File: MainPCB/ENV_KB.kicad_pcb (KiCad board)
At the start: 2 copper layers, 354.6 x 156.2 mm, 201 parts

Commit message: swapped footprint of various parts, updated the logo and tweaked some traces
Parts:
- removed G***: LOGO, EM_Extras:Pattern-Silkscreen
- removed G***: LOGO, EM_Logo:KBLogo
- added D89: 1n4002, Diode_THT:D_DO-35_SOD27_P7.62mm_Horizontal, F.Cu at (227.9, 61.3)
- added kibuzzard-628ADF99 (x2): G***, kibuzzard-628ADF99, F.Cu at (335.3, 172.7)
- added kibuzzard-628AE061 (x3): G***, kibuzzard-628AE061, F.Cu at (357.1, 168.5)
- added kibuzzard-628AE768: G***, kibuzzard-628AE768, F.Cu at (202.7, 66.2)
- added kibuzzard-628AE7EF: G***, kibuzzard-628AE7EF, F.Cu at (310.1, 69.6)
- added kibuzzard-628AE7FB: G***, kibuzzard-628AE7FB, F.Cu at (310.5, 67.0)
- added kibuzzard-628AE805: G***, kibuzzard-628AE805, F.Cu at (310.2, 64.5)
- added kibuzzard-628AE80F: G***, kibuzzard-628AE80F, F.Cu at (310.3, 61.9)
- added kibuzzard-628AE82F: G***, kibuzzard-628AE82F, F.Cu at (320.8, 64.2)
- added kibuzzard-628AE860: G***, kibuzzard-628AE860, F.Cu at (44.3, 69.2)
- added kibuzzard-628AE868: G***, kibuzzard-628AE868, F.Cu at (44.2, 73.2)
- added kibuzzard-628AE874: G***, kibuzzard-628AE874, F.Cu at (44.9, 77.2)
- added kibuzzard-628AE882: G***, kibuzzard-628AE882, F.Cu at (45.0, 81.2)
- added kibuzzard-628AE8A6: G***, kibuzzard-628AE8A6, F.Cu at (44.9, 85.2)
- added kibuzzard-628AE933: G***, kibuzzard-628AE933, F.Cu at (44.8, 89.2)
- added kibuzzard-628AE966: G***, kibuzzard-628AE966, F.Cu at (62.7, 69.2)
- added kibuzzard-628AEA3B: G***, kibuzzard-628AEA3B, F.Cu at (175.4, 64.9)
- added kibuzzard-628AEA3B: G***, kibuzzard-628AEA3B, F.Cu at (180.7, 64.9)
- added kibuzzard-628AEA57: G***, kibuzzard-628AEA57, F.Cu at (186.0, 64.8)
- added kibuzzard-628AEA91: G***, kibuzzard-628AEA91, F.Cu at (202.7, 67.5)
- PowerLED0: value LED 0402 -> LED 3mm; footprint LED_SMD:LED_0402_1005Metric -> LED_THT:LED_D3.0mm
- PowerLedResistor0: value 47K Resistor 0402 -> 47K Resistor; footprint Resistor_SMD:R_0402_1005Metric -> Resistor_THT:R_Axial_DIN0207_L6.3mm_D2.5mm_P7.62mm_Horizontal
- RESISTOR0, RESISTOR1: value 5.1kohm 0402 -> 5.1k; footprint Resistor_SMD:R_0402_1005Metric -> Resistor_THT:R_Axial_DIN0207_L6.3mm_D2.5mm_P7.62mm_Horizontal
- moved RESISTOR1 31.8 mm to (172.7, 62.2), turned to -45 degrees
- moved RESISTOR0 19.2 mm to (183.4, 67.6), turned to 135 degrees
- moved PowerLedResistor0 12.6 mm to (188.6, 67.6), turned to 135 degrees
- moved PowerLED0 7.67 mm to (202.7, 61.5)
- moved kibuzzard-6250C4E7 0.93 mm to (371.0, 62.7)
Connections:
- RPI0 pad 39: unconnected-(RPI0-Pad39) -> VSYS
- RPI0 pad 40: USBVBUS -> unconnected-(RPI0-Pad40)
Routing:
- net GND: track 42.9 -> 76.0 mm, vias 6 -> 5
- net Net-(RESISTOR1-Pad2): track 11.9 -> 38.8 mm
- net Net-(PowerLED0-Pad2): track 1.33 -> 20.7 mm
- net Net-(RESISTOR0-Pad1): track 10.8 -> 29.8 mm
- net USBVBUS: track 29.5 -> 40.8 mm, vias 3 -> 2
- net col15: track 185.1 -> 179.5 mm
- net col4: track 248.1 -> 245.7 mm
- net col2: track 276.3 -> 274.3 mm
- net col0: track 345.0 -> 343.0 mm
- net USB2_N: track 45.2 -> 43.3 mm
- net Net-(D62-Pad2): track 134.2 -> 132.6 mm
- net col6: track 232.4 -> 231.0 mm
- net USB2_P: track 44.9 -> 43.5 mm
- net col10: track 182.2 -> 181.0 mm
- net col3: track 282.7 -> 281.8 mm
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- added copper zone on F.Cu, net (none)
- added copper zone on F.Cu, net VSYS
- removed copper zone on F.Cu, net USBVBUS
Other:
- board text removed: "PWR"
- board text removed: "RESET"

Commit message: various trace tweaks to make the board look more consistent
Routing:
- net USB2_N: track 43.3 -> 48.8 mm
- net Net-(D76-Pad2): track 157.1 -> 161.6 mm
- net Net-(D84-Pad2): track 171.2 -> 175.6 mm
- net Net-(D62-Pad2): track 132.6 -> 136.7 mm
- net Net-(D61-Pad2): track 138.6 -> 142.1 mm
- net Net-(D63-Pad2): track 118.0 -> 121.3 mm
- net Net-(D45-Pad2): track 95.3 -> 98.6 mm
- net Net-(D51-Pad2): track 102.9 -> 106.1 mm
- net Net-(D30-Pad2): track 68.9 -> 72.1 mm
- net Net-(D44-Pad2): track 102.5 -> 105.3 mm
- net Net-(D28-Pad2): track 83.1 -> 85.9 mm
- net Net-(D9-Pad2): track 43.3 -> 45.7 mm
- net Net-(D0-Pad2): track 10.7 -> 12.7 mm
- net Net-(D46-Pad2): track 108.7 -> 110.7 mm
- net Net-(D78-Pad2): track 145.1 -> 146.8 mm
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
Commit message: small tweaks
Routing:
- net Net-(D76-Pad2): track 161.6 -> 167.5 mm
- net USB2_N: track 48.8 -> 52.3 mm
- net Net-(D81-Pad2): track 148.8 -> 147.7 mm
- net Net-(D65-Pad2): track 115.3 -> 116.3 mm
- net Net-(D62-Pad2): track 136.7 -> 135.8 mm
- net col2: track 274.3 -> 275.1 mm
- net col14: track 181.3 -> 181.9 mm
- net Net-(D12-Pad2): track 25.5 -> 26.0 mm

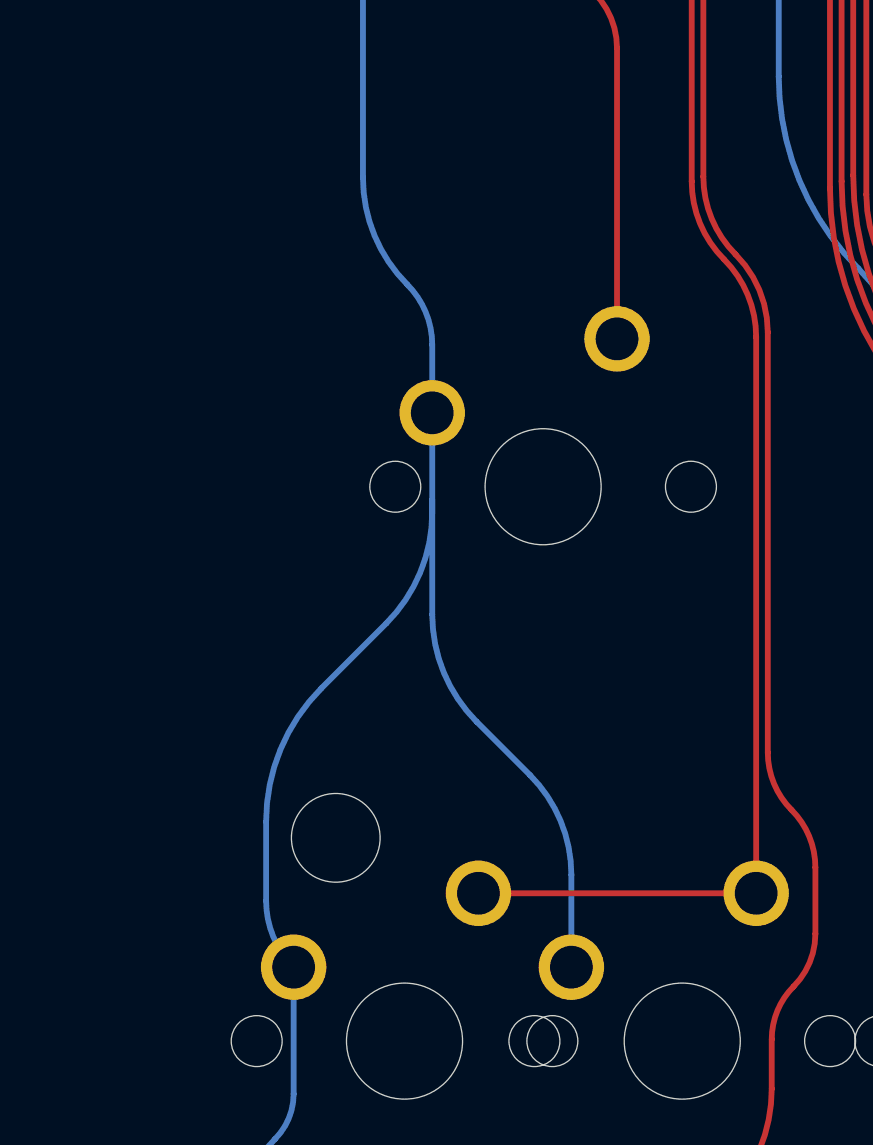
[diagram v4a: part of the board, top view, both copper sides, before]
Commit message: Added Stepped left shift for orig version
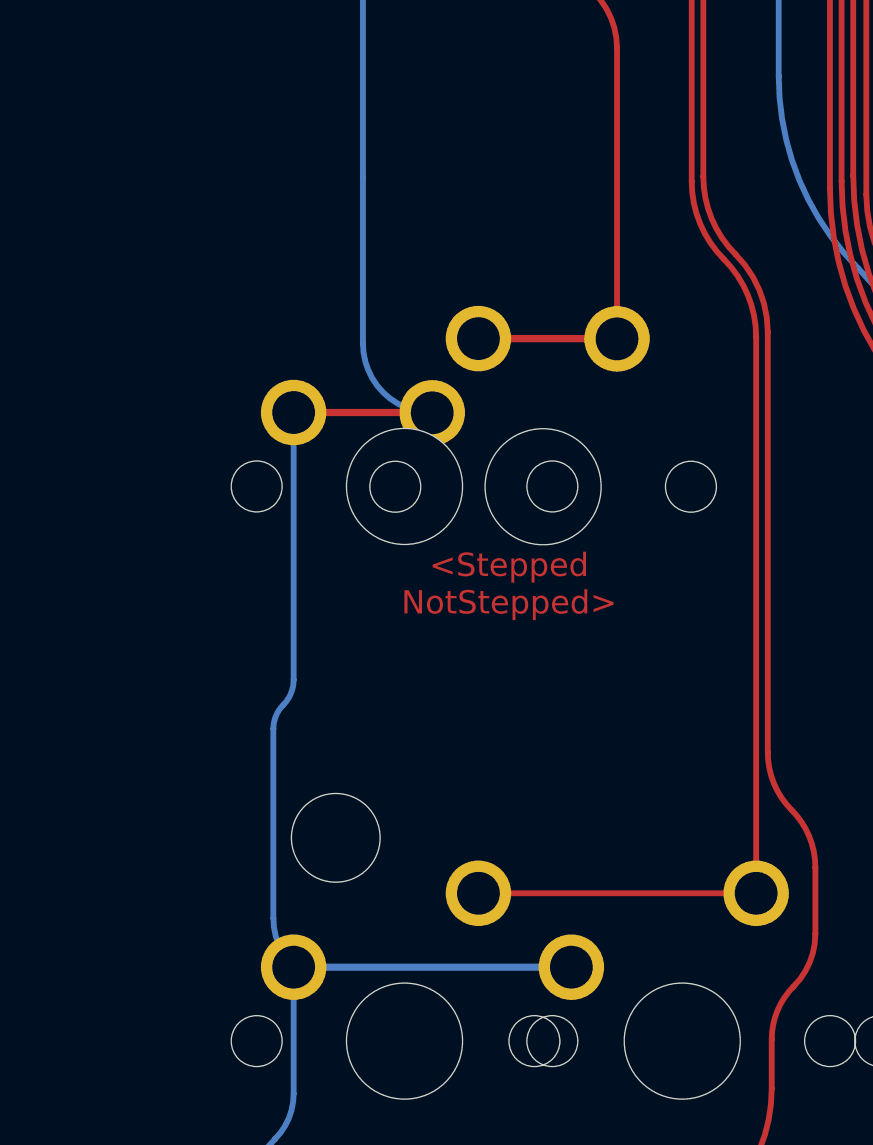
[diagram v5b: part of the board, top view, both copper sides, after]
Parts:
- added K_50A1: KEYSW, MX_Only:MXOnly-1.25U-NoLED, F.Cu at (49.1, 168.4)
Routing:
- net Net-(D50-Pad2): track 95.3 -> 100.0 mm
- net col0: track 343.1 -> 338.9 mm
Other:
- board text added: "<Stepped NotStepped>"
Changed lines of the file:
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@@
       ) (layer "F.SilkS") (width 0) (fill solid))
   )
+  (footprint "MX_Only:MXOnly-1.25U-NoLED" (layer "F.Cu")
+    (at 49.10625 168.45)
+    (property "Sheetfile" "ENV_KB.kicad_sch")
+    (property "Sheetname" "")
+    (attr through_hole)
+    (fp_text reference "K_50A1" (at 0 3.175) (layer "Dwgs.User")
+      (effects (font (size 1 1) (thickness 0.15)))
+    )
+    (fp_text value "KEYSW" (at 0 -7.9375) (layer "Dwgs.User")
+      (effects (font (size 1 1) (thickness 0.15)))
+    )
+    (fp_line (start -7 -7) (end -7 -5) (layer "Dwgs.User") (width 0.15))
+    (fp_line (start -11.90625 -9.525) (end 11.90625 -9.525) (layer "Dwgs.User") (width 0.15))
+    (fp_line (start -5 -7) (end -7 -7) (layer "Dwgs.User") (width 0.15))
+    (fp_line (start -7 5) (end -7 7) (layer "Dwgs.User") (width 0.15))
+    (fp_line (start 5 -7) (end 7 -7) (layer "Dwgs.User") (width 0.15))
+    (fp_line (start -7 7) (end -5 7) (layer "Dwgs.User") (width 0.15))
+    (fp_line (start 5 7) (end 7 7) (layer "Dwgs.User") (width 0.15))
+    (fp_line (start -11.90625 9.525) (end -11.90625 -9.525) (layer "Dwgs.User") (width 0.15))
+    (fp_line (start 7 -7) (end 7 -5) (layer "Dwgs.User") (width 0.15))
+    (fp_line (start 11.90625 -9.525) (end 11.90625 9.525) (layer "Dwgs.User") (width 0.15))
+    (fp_line (start -11.90625 9.525) (end 11.90625 9.525) (layer "Dwgs.User") (width 0.15))
+    (fp_line (start 7 7) (end 7 5) (layer "Dwgs.User") (width 0.15))
+    (pad "" np_thru_hole circle locked (at 5.08 0 48.0996) (size 1.75 1.75) (drill 1.75) (layers *.Cu *.Mask))
+    (pad "" np_thru_hole circle locked (at 0 0) (size 3.9878 3.9878) (drill 3.9878) (layers *.Cu *.Mask))
+    (pad "" np_thru_hole circle locked (at -5.08 0 48.0996) (size 1.75 1.75) (drill 1.75) (layers *.Cu *.Mask))
+    (pad "1" thru_hole circle locked (at -3.81 -2.54) (size 2.25 2.25) (drill 1.47) (layers *.Cu *.Mask)
+      (net 1 "col0") (pinfunction "COL") (pintype "passive"))
+    (pad "2" thru_hole circle locked (at 2.54 -5.08) (size 2.25 2.25) (drill 1.47) (layers *.Cu *.Mask)
+      (net 67 "Net-(D50-Pad2)") (pinfunction "ROW") (pintype "passive"))
+  )
   (footprint "MountingHole:MountingHole_2.2mm_M2_Pad" (layer "F.Cu")
     (at 192.325 63.385)
@@
   (gr_line (start 246.625 78.635) (end 243.125 78.635) (layer "Edge.Cuts") (width 0.1))
   (gr_line (start 216.92804 60.188128) (end 216.925 59.635) (layer "Edge.Cuts") (width 0.1))
+  (gr_text "<Stepped\nNotStepped>" (at 52.7 171.8) (layer "F.Cu")
+    (effects (font (size 0.8 0.8) (thickness 0.15)))
+  )
   (gr_text "https://github.com/Envious-Data/Env-KB" (at 256.225 74.735) (layer "B.Cu")
     (effects (font (size 1 1) (thickness 0.2)) (justify right mirror))
@@
     (style (thickness 0.1) (arrow_length 1.27) (text_position_mode 0) (extension_height 0.58642) (extension_offset 0) keep_text_aligned)
   )
+  (segment (start 45.29625 165.91) (end 50.04875 165.91) (width 0.25) (layer "F.Cu") (net 1))
+  (segment (start 50.04875 165.91) (end 50.05875 165.92) (width 0.25) (layer "F.Cu") (net 1))
+  (segment (start 45.29625 175.09625) (end 45.29625 165.91) (width 0.2) (layer "B.Cu") (net 1))
   (segment (start 244.298792 89.841207) (end 250.54 83.6) (width 0.2) (layer "B.Cu") (net 1))
-  (segment (start 54.84 184.97) (end 54.84 181.799183) (width 0.2) (layer "B.Cu") (net 1))
-  (segment (start 53.42 178.371) (end 51.586454 176.537454) (width 0.2) (layer "B.Cu") (net 1))
+  (segment (start 47.6775 163.53875) (end 47.6775 157.83436) (width 0.2) (layer "B.Cu") (net 1))
   (segment (start 47.915 91.435) (end 240.451036 91.435) (width 0.2) (layer "B.Cu") (net 1))
+  (segment (start 54.84 184.97) (end 45.29625 184.97) (width 0.25) (layer "B.Cu") (net 1))
   (segment (start 42.915 127.82) (end 42.915 99.245) (width 0.2) (layer "B.Cu") (net 1))
-  (segment (start 44.35 182.685551) (end 44.35 179.969871) (width 0.2) (layer "B.Cu") (net 1))
-  (segment (start 50.05875 172.84925) (end 50.05875 168.90125) (width 0.2) (layer "B.Cu") (net 1))
   (segment (start 43.513 199.714854) (end 43.513 193.63183) (width 0.2) (layer "B.Cu") (net 1))
-  (segment (start 50.05875 165.92) (end 50.05875 163.583205) (width 0.2) (layer "B.Cu") (net 1))
   (segment (start 45.29625 189.326666) (end 45.29625 184.97) (width 0.2) (layer "B.Cu") (net 1))
-  (segment (start 50.05875 165.92) (end 50.05875 168.90125) (width 0.2) (layer "B.Cu") (net 1))
   (segment (start 47.6775 157.83436) (end 47.6775 146.87) (width 0.2) (layer "B.Cu") (net 1))
   (segment (start 42.915 134.197812) (end 42.915 127.82) (width 0.2) (layer "B.Cu") (net 1))
-  (segment (start 46.24849 175.38651) (end 48.475 173.16) (width 0.2) (layer "B.Cu") (net 1))
   (segment (start 47.6775 146.87) (end 47.6775 145.695503) (width 0.2) (layer "B.Cu") (net 1))
   (segment (start 42.915 99.245) (end 42.915 96.435) (width 0.2) (layer "B.Cu") (net 1))
-  (segment (start 50.05875 169.33649) (end 50.05875 168.90125) (width 0.2) (layer "B.Cu") (net 1))
-  (arc (start 44.35 179.969871) (mid 44.843402 177.489374) (end 46.24849 175.38651) (width 0.2) (layer "B.Cu") (net 1))
-  (arc (start 50.05875 163.583205) (mid 49.835568 162.461194) (end 49.2 161.51) (width 0.2) (layer "B.Cu") (net 1))
-  (arc (start 48.475 173.16) (mid 49.647146 171.405759) (end 50.05875 169.33649) (width 0.2) (layer "B.Cu") (net 1))
-  (arc (start 49.2 161.51) (mid 48.073184 159.823602) (end 47.6775 157.83436) (width 0.2) (layer "B.Cu") (net 1))
+  (segment (start 44.6 183.289104) (end 44.6 176.777131) (width 0.2) (layer "B.Cu") (net 1))
+  (arc (start 44.937393 175.962607) (mid 45.202986 175.565119) (end 45.29625 175.09625) (width 0.2) (layer "B.Cu") (net 1))
+  (arc (start 44.6 176.777131) (mid 44.687683 176.336319) (end 44.937393 175.962607) (width 0.2) (layer "B.Cu") (net 1))
+  (arc (start 45.29625 184.97) (mid 44.78095 184.198798) (end 44.6 183.289104) (width 0.2) (layer "B.Cu") (net 1))
   (arc (start 43.513 193.63183) (mid 43.809391 192.14177) (end 44.653442 190.878558) (width 0.2) (layer "B.Cu") (net 1))
   (arc (start 45.29625 204.02) (mid 43.976451 202.044783) (end 43.513 199.714854) (width 0.2) (layer "B.Cu") (net 1))
-  (arc (start 51.586454 176.537454) (mid 50.455787 174.845292) (end 50.05875 172.84925) (width 0.2) (layer "B.Cu") (net 1))
   (arc (start 47.6775 145.695503) (mid 47.046613 142.523822) (end 45.25 139.835) (width 0.2) (layer "B.Cu") (net 1))
   (arc (start 47.915 91.435) (mid 44.379466 92.899466) (end 42.915 96.435) (width 0.2) (layer "B.Cu") (net 1))
   (arc (start 44.653442 190.878558) (mid 45.129186 190.166551) (end 45.29625 189.326666) (width 0.2) (layer "B.Cu") (net 1))
   (arc (start 45.25 139.835) (mid 43.521846 137.248636) (end 42.915 134.197812) (width 0.2) (layer "B.Cu") (net 1))
-  (arc (start 54.84 181.799183) (mid 54.470954 179.943864) (end 53.42 178.371) (width 0.2) (layer "B.Cu") (net 1))
-  (arc (start 45.29625 184.97) (mid 44.595922 183.921886) (end 44.35 182.685551) (width 0.2) (layer "B.Cu") (net 1))
   (arc (start 240.451036 91.435) (mid 242.533426 91.020786) (end 244.298792 89.841207) (width 0.2) (layer "B.Cu") (net 1))
+  (arc (start 50.05875 165.92) (mid 48.374952 165.222548) (end 47.6775 163.53875) (width 0.2) (layer "B.Cu") (net 1))
   (segment (start 253.08 83.6) (end 252.214996 84.465003) (width 0.2) (layer "B.Cu") (net 2))
   (segment (start 240.66583 91.885) (end 66.965 91.885) (width 0.2) (layer "B.Cu") (net 2))
@@
   (arc (start 356.575009 80.385009) (mid 356.575 80.385002) (end 356.574993 80.385) (width 0.2) (layer "F.Cu") (net 66))
   (arc (start 377.8775 144.33) (mid 377.066183 142.371307) (end 375.10749 141.55999) (width 0.2) (layer "F.Cu") (net 66))
+  (segment (start 51.64625 163.37) (end 56.39875 163.37) (width 0.25) (layer "F.Cu") (net 67))
   (segment (start 56.175 144.180405) (end 56.175 144.035) (width 0.2) (layer "F.Cu") (net 67))
   (segment (start 55.397182 142.157182) (end 55.30101 142.06101) (width 0.2) (layer "F.Cu") (net 67))
@@
   (segment (start 44.250417 88.283771) (end 44.250417 92.040757) (width 0.2) (layer "F.Cu") (net 67))
   (segment (start 56.40875 163.38) (end 56.40875 153.38863) (width 0.2) (layer "F.Cu") (net 67))
+  (segment (start 56.39875 163.37) (end 56.40875 163.38) (width 0.25) (layer "F.Cu") (net 67))
   (arc (start 55.616875 151.476875) (mid 55.030801 150.599754) (end 54.825 149.565119) (width 0.2) (layer "F.Cu") (net 67))
   (arc (start 55.30101 142.06101) (mid 54.654162 141.092934) (end 54.42702 139.951011) (width 0.2) (layer "F.Cu") (net 67))
